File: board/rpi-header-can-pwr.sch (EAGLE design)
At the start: 31 parts, among them U1 MCP2515, X1 RJ45-8L21-S, X2 RJ45-8L21-S

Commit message: board - minor adjustments
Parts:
- removed JP3: (no value), pinhead:PINHD-1X2
- added J1: (no value), SparkFun-Connectors:CONN_023.5MM
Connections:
- net GND: now also J1.1; no longer JP3.1
- net N$5: now also J1.2; no longer JP3.2
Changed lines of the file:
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@@
 <part name="R4" library="rcl" deviceset="R-EU_" device="R0603" value="1k"/>
 <part name="GND16" library="supply1" deviceset="GND" device=""/>
-<part name="JP3" library="pinhead" deviceset="PINHD-1X2" device=""/>
 <part name="P+11" library="supply1" deviceset="+12V" device=""/>
 <part name="GND18" library="supply1" deviceset="GND" device=""/>
 <part name="F3" library="fuse" deviceset="LITTLEFUSE" device=""/>
 <part name="F5" library="fuse" deviceset="FUSE" device="TE5"/>
+<part name="J1" library="SparkFun-Connectors" deviceset="CONN_02" device="3.5MM"/>
 </parts>
 <sheets>
@@
 <instance part="R4" gate="G$1" x="101.6" y="106.68" rot="R270"/>
 <instance part="GND16" gate="1" x="101.6" y="93.98"/>
-<instance part="JP3" gate="G$1" x="152.4" y="78.74" rot="R180"/>
 <instance part="P+11" gate="1" x="193.04" y="78.74" rot="R270"/>
 <instance part="GND18" gate="1" x="187.96" y="76.2" rot="R90"/>
 <instance part="F3" gate="A" x="172.72" y="78.74"/>
 <instance part="F5" gate="G$1" x="187.96" y="43.18"/>
+<instance part="J1" gate="G$1" x="152.4" y="76.2"/>
 </instances>
 <busses>
@@
 </segment>
 <segment>
-<pinref part="JP3" gate="G$1" pin="1"/>
 <pinref part="GND18" gate="1" pin="GND"/>
-<wire x1="154.94" y1="76.2" x2="185.42" y2="76.2" width="0.1524" layer="91"/>
+<wire x1="160.02" y1="76.2" x2="185.42" y2="76.2" width="0.1524" layer="91"/>
+<pinref part="J1" gate="G$1" pin="1"/>
 </segment>
 </net>
@@
 <net name="N$5" class="0">
 <segment>
-<pinref part="JP3" gate="G$1" pin="2"/>
-<wire x1="167.64" y1="78.74" x2="154.94" y2="78.74" width="0.1524" layer="91"/>
+<wire x1="167.64" y1="78.74" x2="160.02" y2="78.74" width="0.1524" layer="91"/>
 <pinref part="F3" gate="A" pin="1"/>
-</segment>
-</net>
+<pinref part="J1" gate="G$1" pin="2"/>
+</segment>
+</net>

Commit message: add tamper
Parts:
- added C12: 10nF, eagle-ltspice:CC0402
- added D18: BAS70-04, diode:BAS70-04
- added GND84: (no value), SparkFun-Connectors:CONN_023.5MM
- added R59: 10k, rcl:R-EU_R0402
- added R60, R61: 100, rcl:R-EU_R0402
- added R62: 1k, rcl:R-EU_R0402
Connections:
- removed net GPIO17: RPI1.GPIO17
- removed net GPIO5: RPI1.GPIO5
- new net ASDASD: D18.C1A2, R61.1, R62.2
- new net N$10: GND84.2, R60.1
- new net N$11: C12.2, GND84.1, R59.1, R62.1
- new net TAMPER: R61.2, RPI1.GPIO17
- net +3V3: now also D18.C2, R60.2
- net GND: now also C12.1, D18.A1, R59.2
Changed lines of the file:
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@@
 <part name="F5" library="fuse" deviceset="FUSE" device="TE5"/>
 <part name="J1" library="SparkFun-Connectors" deviceset="CONN_02" device="3.5MM"/>
+<part name="GND84" library="SparkFun-Connectors" deviceset="CONN_02" device="3.5MM"/>
+<part name="+3V30" library="supply1" deviceset="+3V3" device=""/>
+<part name="GND85" library="supply1" deviceset="GND" device=""/>
+<part name="R59" library="rcl" deviceset="R-EU_" device="R0402" value="10k"/>
+<part name="GND86" library="supply1" deviceset="GND" device=""/>
+<part name="C12" library="eagle-ltspice" deviceset="C" device="C0402" value="10nF"/>
+<part name="D18" library="diode" deviceset="BAS70-04" device=""/>
+<part name="+3V31" library="supply1" deviceset="+3V3" device=""/>
+<part name="GND87" library="supply1" deviceset="GND" device=""/>
+<part name="R60" library="rcl" deviceset="R-EU_" device="R0402" value="100"/>
+<part name="R61" library="rcl" deviceset="R-EU_" device="R0402" value="100"/>
+<part name="R62" library="rcl" deviceset="R-EU_" device="R0402" value="1k"/>
 </parts>
 <sheets>
@@
 <instance part="+3V4" gate="G$1" x="0" y="73.66"/>
 <instance part="P+8" gate="G$1" x="78.74" y="66.04" rot="MR90"/>
+<instance part="GND84" gate="G$1" x="-38.1" y="83.82" rot="R180"/>
+<instance part="+3V30" gate="G$1" x="-71.12" y="81.28" rot="R90"/>
+<instance part="GND85" gate="1" x="-48.26" y="99.06" rot="R180"/>
+<instance part="R59" gate="G$1" x="-48.26" y="88.9" rot="R90"/>
+<instance part="GND86" gate="1" x="-63.5" y="99.06" rot="R180"/>
+<instance part="C12" gate="G$1" x="-63.5" y="91.44"/>
+<instance part="D18" gate="G$1" x="-83.82" y="99.06" rot="R180"/>
+<instance part="+3V31" gate="G$1" x="-96.52" y="99.06" rot="R90"/>
+<instance part="GND87" gate="1" x="-73.66" y="99.06" rot="R90"/>
+<instance part="R60" gate="G$1" x="-53.34" y="81.28" rot="R180"/>
+<instance part="R61" gate="G$1" x="-111.76" y="83.82" rot="R180"/>
+<instance part="R62" gate="G$1" x="-73.66" y="83.82" rot="R180"/>
 </instances>
 <busses>
@@
 </segment>
 </net>
-<net name="GPIO17" class="0">
-<segment>
-<pinref part="RPI1" gate="G$1" pin="GPIO17"/>
-<wire x1="15.24" y1="53.34" x2="2.54" y2="53.34" width="0.1524" layer="91"/>
-<label x="2.54" y="53.34" size="1.778" layer="95"/>
-</segment>
-</net>
 <net name="GPIO27" class="0">
 <segment>
@@
 </segment>
 </net>
-<net name="GPIO5" class="0">
-<segment>
-<pinref part="RPI1" gate="G$1" pin="GPIO5"/>
-<wire x1="2.54" y1="30.48" x2="15.24" y2="30.48" width="0.1524" layer="91"/>
-<label x="2.54" y="30.48" size="1.778" layer="95"/>
+<net name="TAMPER" class="0">
+<segment>
+<pinref part="R61" gate="G$1" pin="2"/>
+<wire x1="-116.84" y1="83.82" x2="-124.46" y2="83.82" width="0.1524" layer="91"/>
+<label x="-124.46" y="83.82" size="1.778" layer="95" rot="R180" xref="yes"/>
+</segment>
+<segment>
+<pinref part="RPI1" gate="G$1" pin="GPIO17"/>
+<label x="2.54" y="53.34" size="1.778" layer="95"/>
+<wire x1="15.24" y1="53.34" x2="-12.7" y2="53.34" width="0.1524" layer="91"/>
+<label x="-12.7" y="53.34" size="1.778" layer="95" rot="R180" xref="yes"/>
 </segment>
 </net>
@@
 <junction x="-53.34" y="119.38"/>
 </segment>
+<segment>
+<pinref part="GND85" gate="1" pin="GND"/>
+<pinref part="R59" gate="G$1" pin="2"/>
+<wire x1="-48.26" y1="96.52" x2="-48.26" y2="93.98" width="0.1524" layer="91"/>
+</segment>
+<segment>
+<pinref part="GND86" gate="1" pin="GND"/>
+<pinref part="C12" gate="G$1" pin="1"/>
+<wire x1="-63.5" y1="96.52" x2="-63.5" y2="93.98" width="0.1524" layer="91"/>
+</segment>
+<segment>
+<pinref part="D18" gate="G$1" pin="A1"/>
+<pinref part="GND87" gate="1" pin="GND"/>
+<wire x1="-78.74" y1="99.06" x2="-76.2" y2="99.06" width="0.1524" layer="91"/>
+</segment>
 </net>
 <net name="TXD" class="0">
@@
 <pinref part="+3V4" gate="G$1" pin="+3V3"/>
 </segment>
+<segment>
+<pinref part="+3V31" gate="G$1" pin="+3V3"/>
+<pinref part="D18" gate="G$1" pin="C2"/>
+<wire x1="-93.98" y1="99.06" x2="-88.9" y2="99.06" width="0.1524" layer="91"/>
+</segment>
+<segment>
+<pinref part="R60" gate="G$1" pin="2"/>
+<pinref part="+3V30" gate="G$1" pin="+3V3"/>
+<wire x1="-58.42" y1="81.28" x2="-68.58" y2="81.28" width="0.1524" layer="91"/>
+</segment>
 </net>
 <net name="5V" class="0">
@@
 </segment>
 </net>
+<net name="ASDASD" class="0">
+<segment>
+<pinref part="D18" gate="G$1" pin="C1A2"/>
+<wire x1="-83.82" y1="96.52" x2="-83.82" y2="83.82" width="0.1524" layer="91"/>
+<wire x1="-83.82" y1="83.82" x2="-106.68" y2="83.82" width="0.1524" layer="91"/>
+<pinref part="R61" gate="G$1" pin="1"/>
+<pinref part="R62" gate="G$1" pin="2"/>
+<wire x1="-78.74" y1="83.82" x2="-83.82" y2="83.82" width="0.1524" layer="91"/>
+<junction x="-83.82" y="83.82"/>
+</segment>
+</net>
+<net name="N$10" class="0">
+<segment>
+<pinref part="R60" gate="G$1" pin="1"/>
+<pinref part="GND84" gate="G$1" pin="2"/>
+<wire x1="-48.26" y1="81.28" x2="-45.72" y2="81.28" width="0.1524" layer="91"/>
+</segment>
+</net>
+<net name="N$11" class="0">
+<segment>
+<pinref part="C12" gate="G$1" pin="2"/>
+<wire x1="-63.5" y1="86.36" x2="-63.5" y2="83.82" width="0.1524" layer="91"/>
+<pinref part="R59" gate="G$1" pin="1"/>
+<wire x1="-48.26" y1="83.82" x2="-63.5" y2="83.82" width="0.1524" layer="91"/>
+<junction x="-48.26" y="83.82"/>
+<pinref part="GND84" gate="G$1" pin="1"/>
+<wire x1="-45.72" y1="83.82" x2="-48.26" y2="83.82" width="0.1524" layer="91"/>
+<pinref part="R62" gate="G$1" pin="1"/>
+<wire x1="-68.58" y1="83.82" x2="-63.5" y2="83.82" width="0.1524" layer="91"/>
+<junction x="-63.5" y="83.82"/>
+</segment>
+</net>

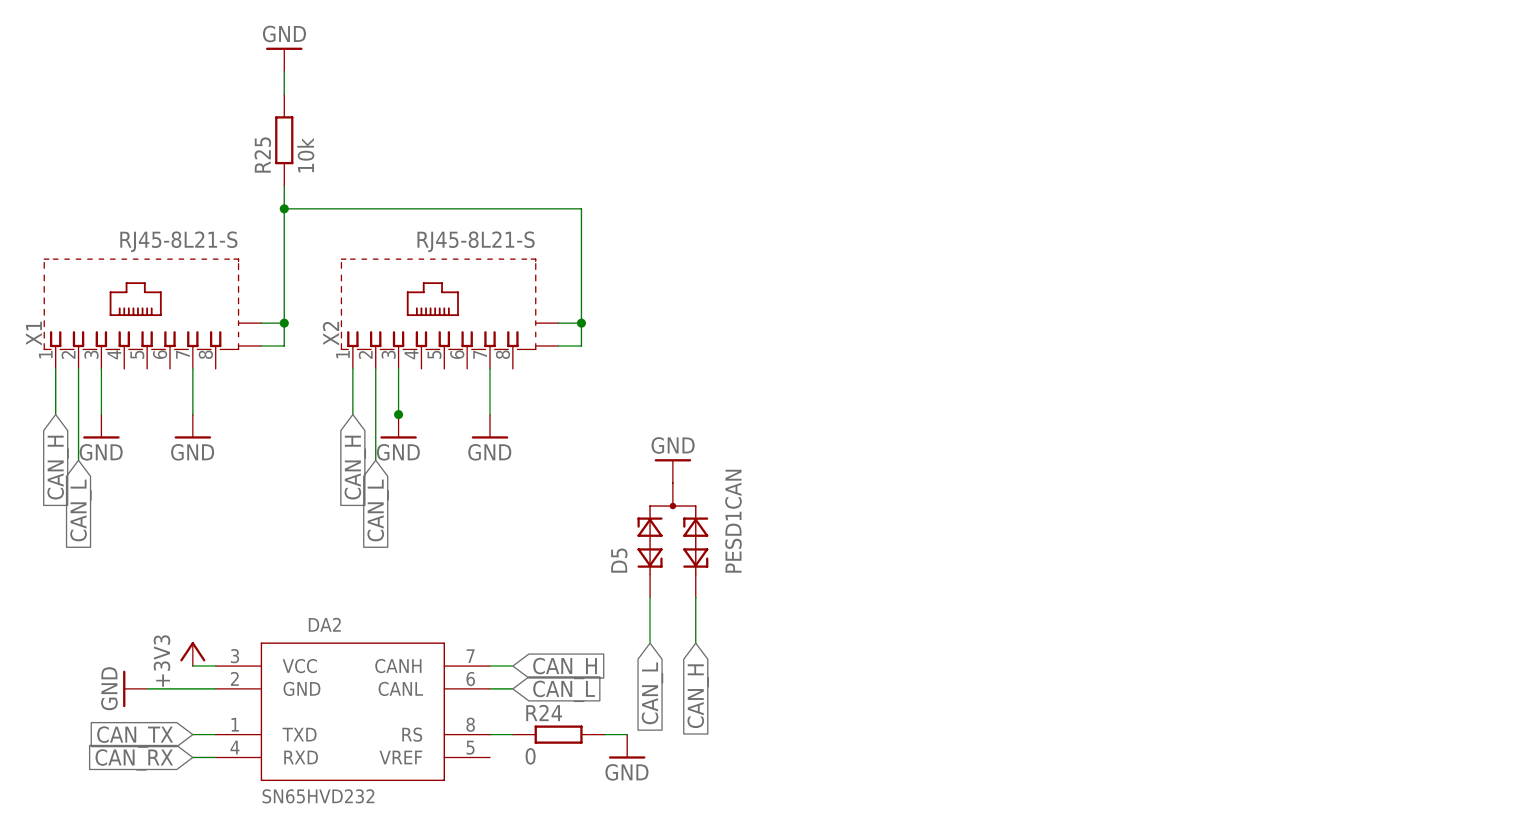
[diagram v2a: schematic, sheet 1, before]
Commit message: power over can
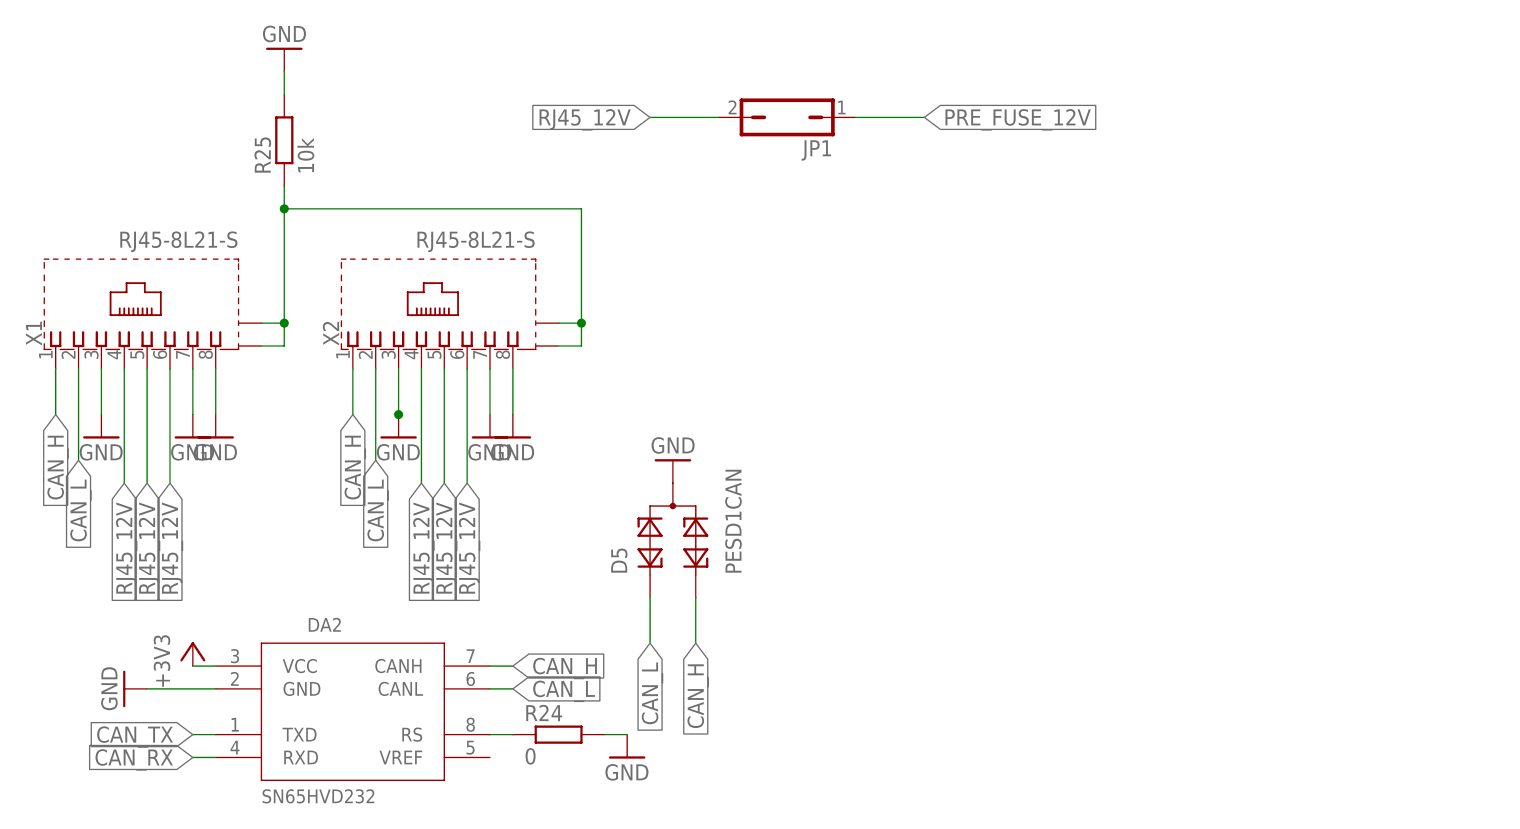
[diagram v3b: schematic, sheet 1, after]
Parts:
- added JP1: (no value), jumper:JP1Q
- C12: device eagle-ltspice:CC0402 -> eagle-ltspice:CC0603
- R59, R60, R61, R62: device rcl:R-EU_R0402 -> rcl:R-EU_R0603
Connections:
- removed net N$5: F3.1, J1.2
- new net PRE_FUSE_12V: F3.1, J1.2, JP1.1
- new net RJ45_12V: JP1.2, X1.4, X1.5, X1.6, X2.4, X2.5, X2.6
- net GND: now also X1.8, X2.8

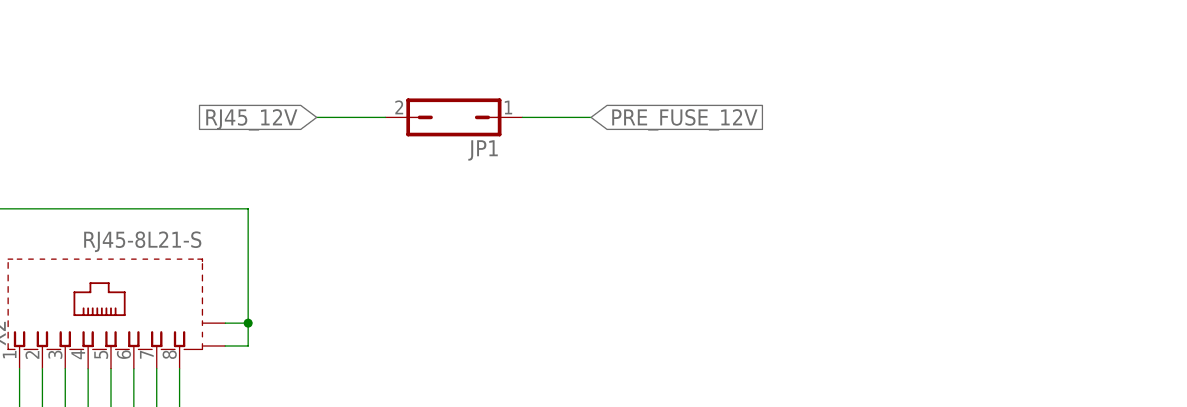
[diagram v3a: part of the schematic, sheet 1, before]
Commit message: extra fuse for power over can
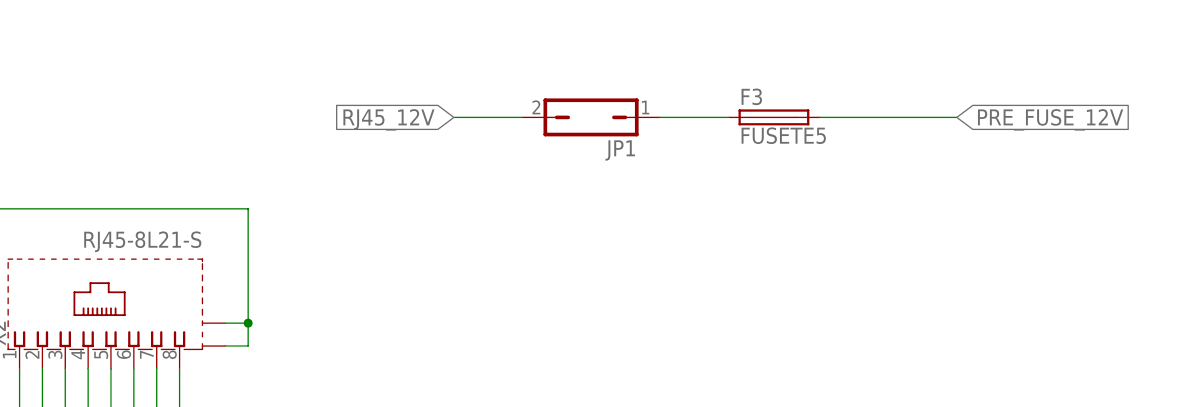
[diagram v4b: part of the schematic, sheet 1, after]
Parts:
- removed F5: FUSETE5, fuse:FUSETE5
- added F1: FUSETE5, fuse:FUSETE5
- added F2: FUSELITTLEFUSE, fuse:FUSELITTLEFUSE
- F3: value (none) -> FUSETE5; device fuse:LITTLEFUSE -> fuse:FUSETE5
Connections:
- new net N$5: F3.1, JP1.1
- net +12V: now also F1.2; no longer F3.2
- net 5V: now also F2.2; no longer F5.2
- net N$8: now also F2.1; no longer F5.1
- net PRE_FUSE_12V: now also F1.1, F3.2; no longer F3.1, JP1.1
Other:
- moved on the sheet: JP1
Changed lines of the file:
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@@
 <part name="P+11" library="supply1" deviceset="+12V" device=""/>
 <part name="GND18" library="supply1" deviceset="GND" device=""/>
-<part name="F3" library="fuse" deviceset="LITTLEFUSE" device=""/>
-<part name="F5" library="fuse" deviceset="FUSE" device="TE5"/>
 <part name="J1" library="SparkFun-Connectors" deviceset="CONN_02" device="3.5MM"/>
 <part name="GND84" library="SparkFun-Connectors" deviceset="CONN_02" device="3.5MM"/>
@@
 <part name="GND19" library="supply1" deviceset="GND" device=""/>
 <part name="JP1" library="jumper" deviceset="JP1Q" device=""/>
+<part name="F1" library="fuse" deviceset="FUSE" device="TE5"/>
+<part name="F2" library="fuse" deviceset="FUSE" device="LITTLEFUSE"/>
+<part name="F3" library="fuse" deviceset="FUSE" device="TE5"/>
 </parts>
 <sheets>
@@
 <instance part="GND17" gate="1" x="-109.22" y="-22.86"/>
 <instance part="GND19" gate="1" x="-76.2" y="-22.86"/>
-<instance part="JP1" gate="A" x="-45.72" y="12.7" rot="R90"/>
+<instance part="JP1" gate="A" x="-30.48" y="12.7" rot="R90"/>
+<instance part="F3" gate="G$1" x="-10.16" y="12.7"/>
 </instances>
 <busses>
@@
 <segment>
 <pinref part="JP1" gate="A" pin="2"/>
-<wire x1="-53.34" y1="12.7" x2="-60.96" y2="12.7" width="0.1524" layer="91"/>
-<label x="-60.96" y="12.7" size="1.778" layer="95" rot="R180" xref="yes"/>
+<wire x1="-38.1" y1="12.7" x2="-45.72" y2="12.7" width="0.1524" layer="91"/>
+<label x="-45.72" y="12.7" size="1.778" layer="95" rot="R180" xref="yes"/>
+</segment>
+</net>
+<net name="N$5" class="0">
+<segment>
+<pinref part="JP1" gate="A" pin="1"/>
+<pinref part="F3" gate="G$1" pin="1"/>
+<wire x1="-22.86" y1="12.7" x2="-15.24" y2="12.7" width="0.1524" layer="91"/>
 </segment>
 </net>
 <net name="PRE_FUSE_12V" class="0">
 <segment>
-<pinref part="JP1" gate="A" pin="1"/>
-<wire x1="-38.1" y1="12.7" x2="-30.48" y2="12.7" width="0.1524" layer="91"/>
-<label x="-30.48" y="12.7" size="1.778" layer="95" xref="yes"/>
+<pinref part="F3" gate="G$1" pin="2"/>
+<wire x1="-5.08" y1="12.7" x2="10.16" y2="12.7" width="0.1524" layer="91"/>
+<label x="10.16" y="12.7" size="1.778" layer="95" xref="yes"/>
 </segment>
 </net>
@@
 <instance part="P+11" gate="1" x="193.04" y="78.74" rot="R270"/>
 <instance part="GND18" gate="1" x="187.96" y="76.2" rot="R90"/>
-<instance part="F3" gate="A" x="172.72" y="78.74"/>
-<instance part="F5" gate="G$1" x="187.96" y="43.18"/>
 <instance part="J1" gate="G$1" x="152.4" y="76.2"/>
+<instance part="F1" gate="G$1" x="172.72" y="78.74"/>
+<instance part="F2" gate="G$1" x="187.96" y="43.18"/>
 </instances>
 <busses>
@@
 <pinref part="P+11" gate="1" pin="+12V"/>
 <wire x1="177.8" y1="78.74" x2="190.5" y2="78.74" width="0.1524" layer="91"/>
-<pinref part="F3" gate="A" pin="2"/>
+<pinref part="F1" gate="G$1" pin="2"/>
 </segment>
 </net>
@@
 <pinref part="P+7" gate="G$1" pin="5V"/>
 <wire x1="193.04" y1="43.18" x2="203.2" y2="43.18" width="0.1524" layer="91"/>
-<pinref part="F5" gate="G$1" pin="2"/>
+<pinref part="F2" gate="G$1" pin="2"/>
 </segment>
 </net>
@@
 <segment>
 <wire x1="167.64" y1="78.74" x2="160.02" y2="78.74" width="0.1524" layer="91"/>
-<pinref part="F3" gate="A" pin="1"/>
 <pinref part="J1" gate="G$1" pin="2"/>
+<pinref part="F1" gate="G$1" pin="1"/>
 </segment>
 </net>
@@
 <pinref part="C11" gate="G$1" pin="1"/>
 <wire x1="182.88" y1="43.18" x2="172.72" y2="43.18" width="0.1524" layer="91"/>
-<pinref part="F5" gate="G$1" pin="1"/>
-</segment>
-</net>
+<pinref part="F2" gate="G$1" pin="1"/>
+</segment>
+</net>

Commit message: 3.5mm to 5mm screw terminal
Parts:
- J1: device SparkFun-Connectors:CONN_023.5MM -> SparkFun-Connectors:CONN_025MM
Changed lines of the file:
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@@
 <part name="P+11" library="supply1" deviceset="+12V" device=""/>
 <part name="GND18" library="supply1" deviceset="GND" device=""/>
-<part name="J1" library="SparkFun-Connectors" deviceset="CONN_02" device="3.5MM"/>
+<part name="J1" library="SparkFun-Connectors" deviceset="CONN_02" device="5MM"/>
 <part name="GND84" library="SparkFun-Connectors" deviceset="CONN_02" device="3.5MM"/>
 <part name="+3V30" library="supply1" deviceset="+3V3" device=""/>
